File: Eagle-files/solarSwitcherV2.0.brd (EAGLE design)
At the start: 102.4 x 111.9 mm, 12 parts, among them T1 2N3440

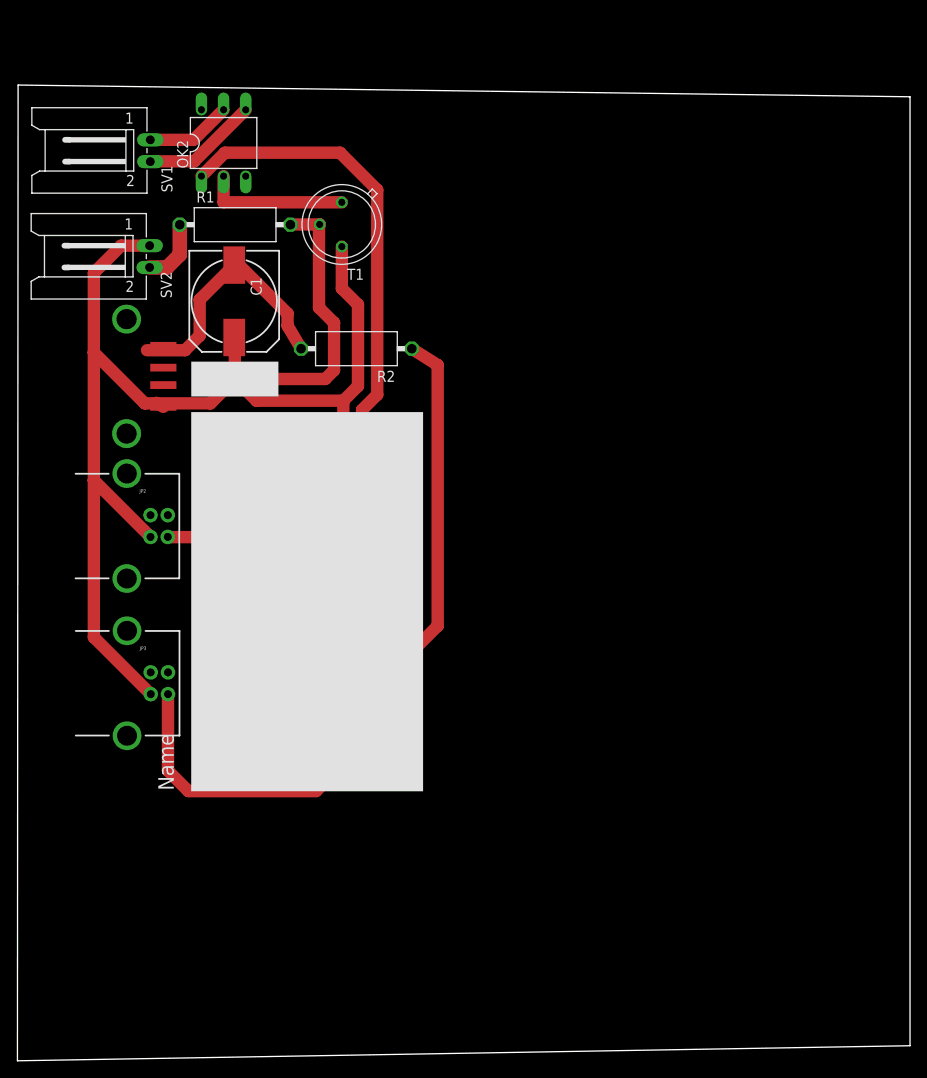
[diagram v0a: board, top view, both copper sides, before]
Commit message: Removed relay-board and replaced with seperate relay and diode
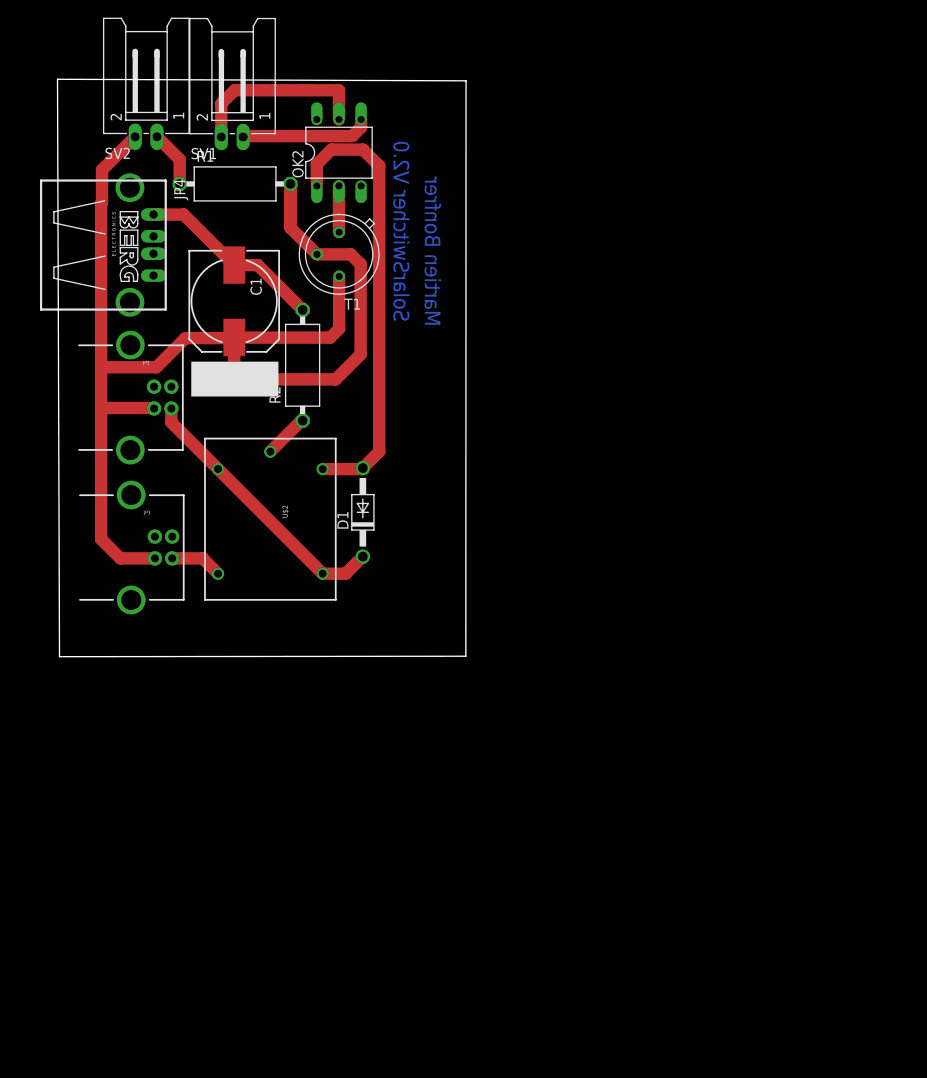
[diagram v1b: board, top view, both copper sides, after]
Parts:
- removed U$1: RELAY_BOARD, MBLIB:RELAY_BOARD
- added D1: 1N4004, diode:DO41-10
- added U$2: RELAYPTH, SRD-05VDC-SL-C:SRD-05VDC-SL-C
- JP4: value USB-A-SMD -> PN87520-S; device SparkFun-Connectors:USB-A-S-NOSILK-FEMALE -> con-berg:PN87520-S
- moved SV2 20.8 mm to (12.4, 81.7), turned to 0 degrees
- moved SV1 17.5 mm to (22.3, 81.6), turned to 0 degrees
- moved JP3 15.6 mm to (13.4, 28.3)
- moved JP4 15.1 mm to (10.5, 63.0), turned to 270 degrees
- moved JP2 14.7 mm to (13.3, 45.5)
- moved OK2 13.3 mm to (34.5, 73.6)
- moved R2 6.46 mm to (30.3, 49.2), turned to 90 degrees
- moved R1 4.67 mm to (22.6, 70.0)
- moved T1 3.44 mm to (34.5, 61.9)
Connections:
- removed net N$9: OK2.4, SV1.2
- new net N$12: D1.C, JP2.VBUS, U$2.COIL0, U$2.SWOPEN
- net GND: now also SV2.2; no longer JP4.GND, SV2.1, U$1.CTRL_GND
- net N$10: now also U$2.SWCOMMON; no longer U$1.RELAY_BASE
- net N$2: now also JP4.1; no longer JP4.VBUS
- net N$3: now also D1.A, U$2.COIL1; no longer U$1.CTRL_IN
- net N$4: now also OK2.4, SV1.1; no longer JP2.VBUS, U$1.CTRL_VCC, U$1.P$2
- net N$5: now also SV2.1; no longer SV2.2
- net N$6: now also U$2.SWCLOSED; no longer U$1.RELAY_STD_ON
- net N$7: now also SV1.2; no longer SV1.1
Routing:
- net N$10: track 54.6 -> 5.17 mm
- net N$4: track 55.8 -> 14.9 mm
- net N$12: track 0.00 -> 31.6 mm
- net GND: track 130.5 -> 101.1 mm
- net N$6: track 32.4 -> 5.99 mm
- net N$9: track 13.4 -> 0.00 mm
- net N$1: track 29.6 -> 42.4 mm
- net N$7: track 9.83 -> 21.3 mm
- net N$8: track 16.6 -> 5.32 mm
- net N$2: track 29.3 -> 21.6 mm
- net N$3: track 52.3 -> 51.2 mm
- net N$5: track 7.51 -> 6.49 mm
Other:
- board size 102.4 x 111.9 mm -> 46.9 x 66.2 mm
- board text added: "Martien Bonfrer"
- board text added: "SolarSwitcher V2.0"

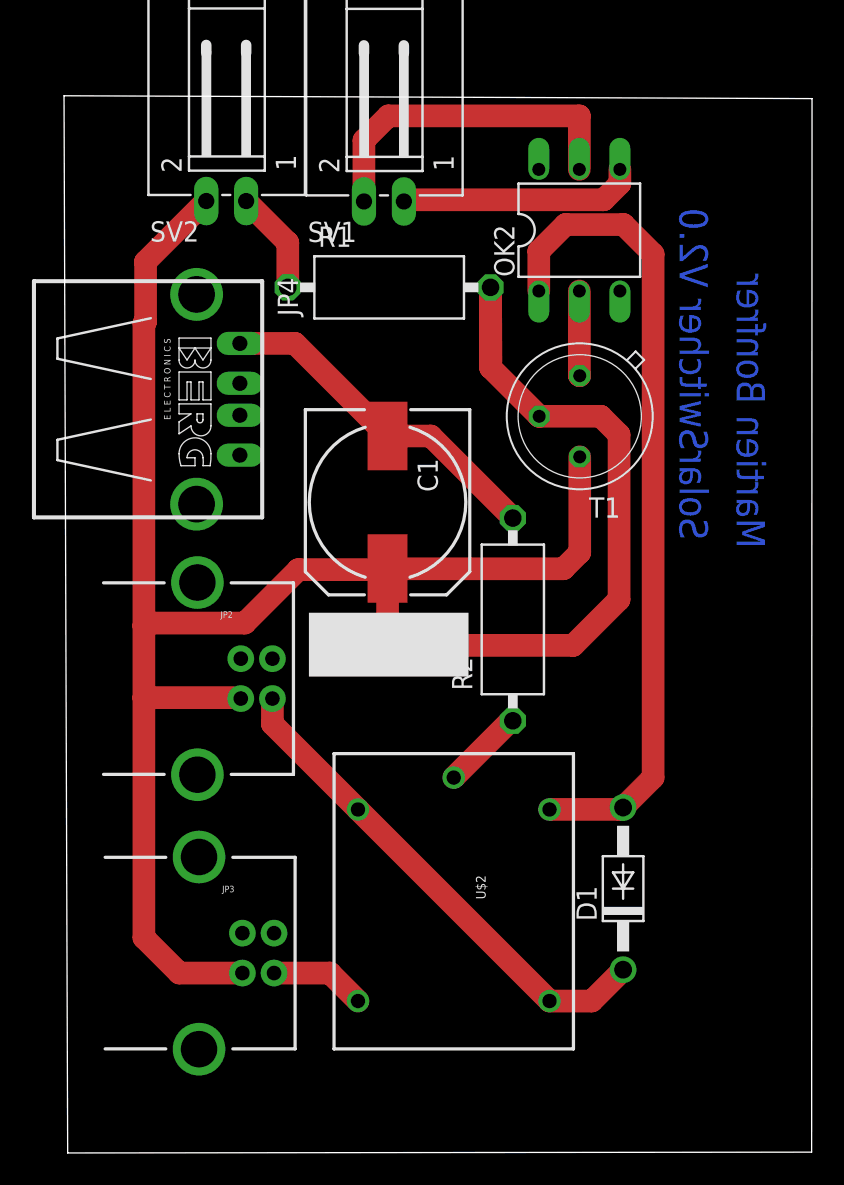
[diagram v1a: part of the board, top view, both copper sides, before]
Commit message: Added status leds
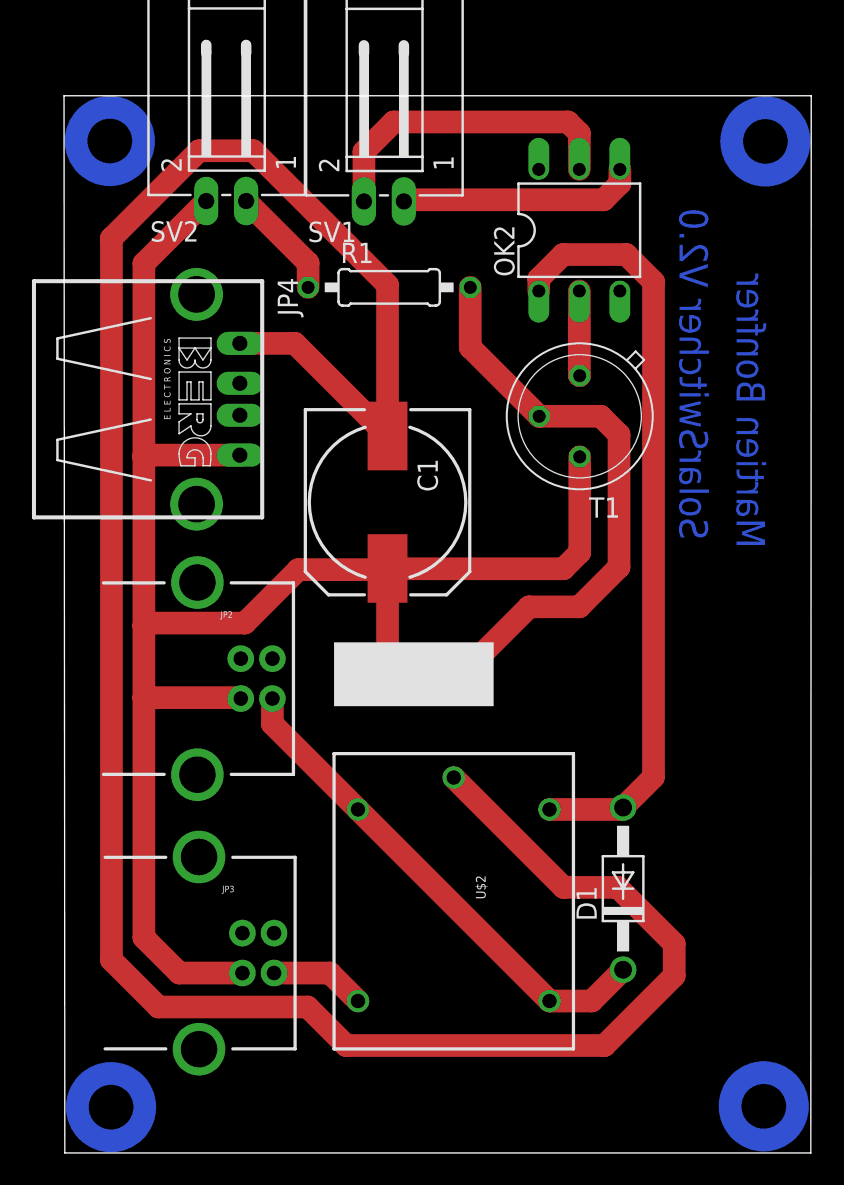
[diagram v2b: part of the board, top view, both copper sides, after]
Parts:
- removed R2: (no value), resistor:VMTB60
- R1: device resistor:VMTB60 -> resistor:0207/10
- moved U$5 2.43 mm to (19.1, 43.8)
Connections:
- removed net N$10: R2.1, U$2.SWCOMMON
- net GND: now also JP4.4
- net N$2: now also U$2.SWCOMMON; no longer R2.2
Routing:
- net N$2: track 21.6 -> 148.8 mm
- net GND: track 101.1 -> 109.7 mm
- net N$1: track 42.4 -> 36.3 mm
- net N$10: track 5.17 -> 0.00 mm
- net N$3: track 51.2 -> 47.6 mm
- net N$7: track 21.3 -> 19.9 mm
- net N$5: track 6.49 -> 7.02 mm
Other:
- board size 46.9 x 66.2 mm -> 46.8 x 66.2 mm

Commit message: Added missing leds
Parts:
- added GREEN_LED, RED_LED: (no value), led:LED5MM
- added R2: 150, resistor:0207/10
- added R3: 180, resistor:0207/10
- C1: value (none) -> 0,22uF
- R1: value (none) -> 10k
- U$5: value POT_TRIMMER -> 20k
- moved SV1 3.20 mm to (25.5, 81.7)
- moved SV2 3.15 mm to (15.5, 81.7)
- turned T1 to 0 degrees
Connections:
- removed net GND: C1.+, JP2.GND, JP3.GND, JP4.4, SV2.2, T1.3, U$5.IN
- new net N$10: D1.A, R3.1, U$2.COIL1
- new net N$13: GREEN_LED.A, R2.2
- new net N$14: R3.2, RED_LED.A
- new net N$9: OK2.2, T1.3
- net N$2: now also R2.1
- net N$3: now also RED_LED.K; no longer D1.A, U$2.COIL1
- net N$8: now also C1.+, GREEN_LED.K, JP2.GND, JP3.GND, JP4.4, SV2.2, U$5.IN; no longer OK2.2
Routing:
- net N$8: track 5.32 -> 121.8 mm
- net GND: track 109.7 -> 0.00 mm
- net N$13: track 0.00 -> 31.4 mm
- net N$3: track 47.6 -> 37.3 mm
- net N$14: track 0.00 -> 6.98 mm
- net N$10: track 0.00 -> 6.96 mm
- net N$2: track 148.8 -> 155.3 mm
- net N$9: track 0.00 -> 5.32 mm
- net N$4: track 14.9 -> 11.1 mm
- net N$7: track 19.9 -> 16.8 mm
- net N$5: track 7.02 -> 5.71 mm
- net N$1: track 36.3 -> 35.2 mm
